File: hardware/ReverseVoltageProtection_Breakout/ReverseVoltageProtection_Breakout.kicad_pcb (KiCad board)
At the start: 2 copper layers, 33.5 x 17.8 mm, 5 parts, among them Q1 Q_PMOS_DGS

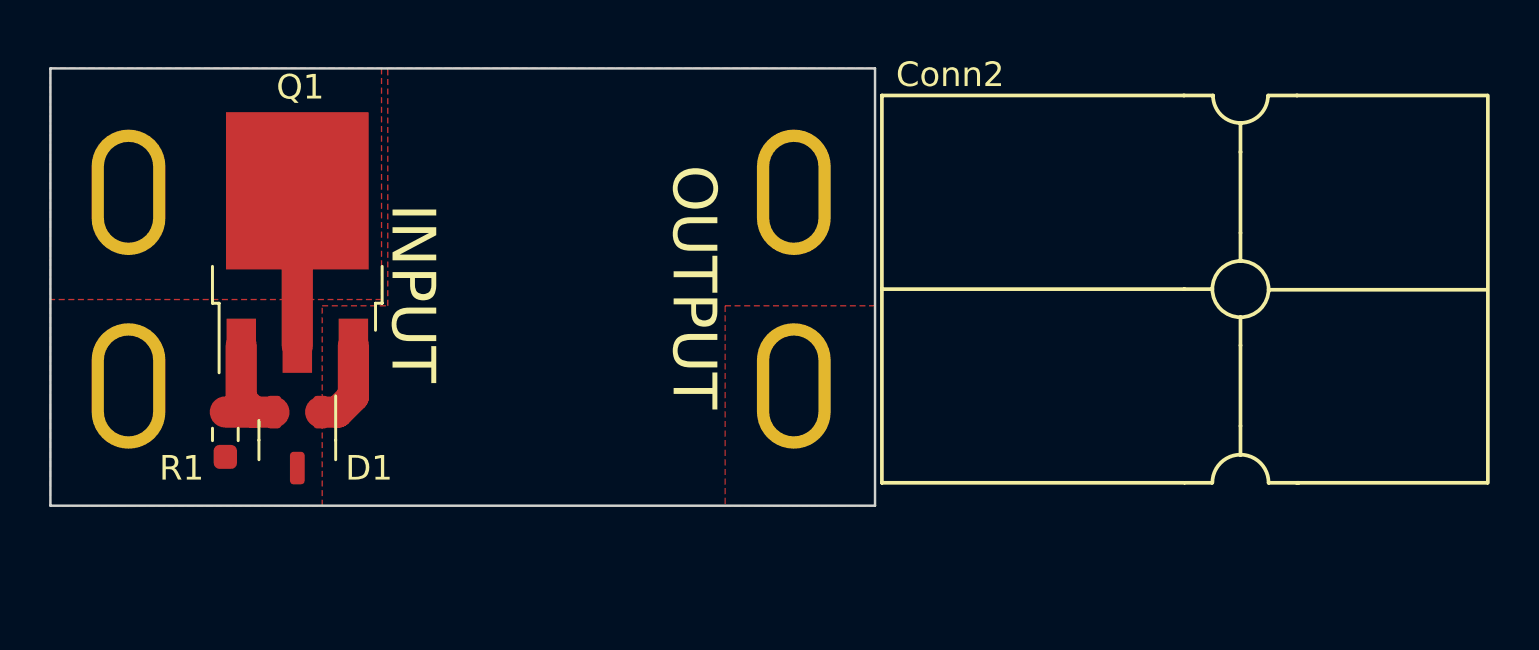
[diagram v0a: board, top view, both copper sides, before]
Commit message: made 12V version
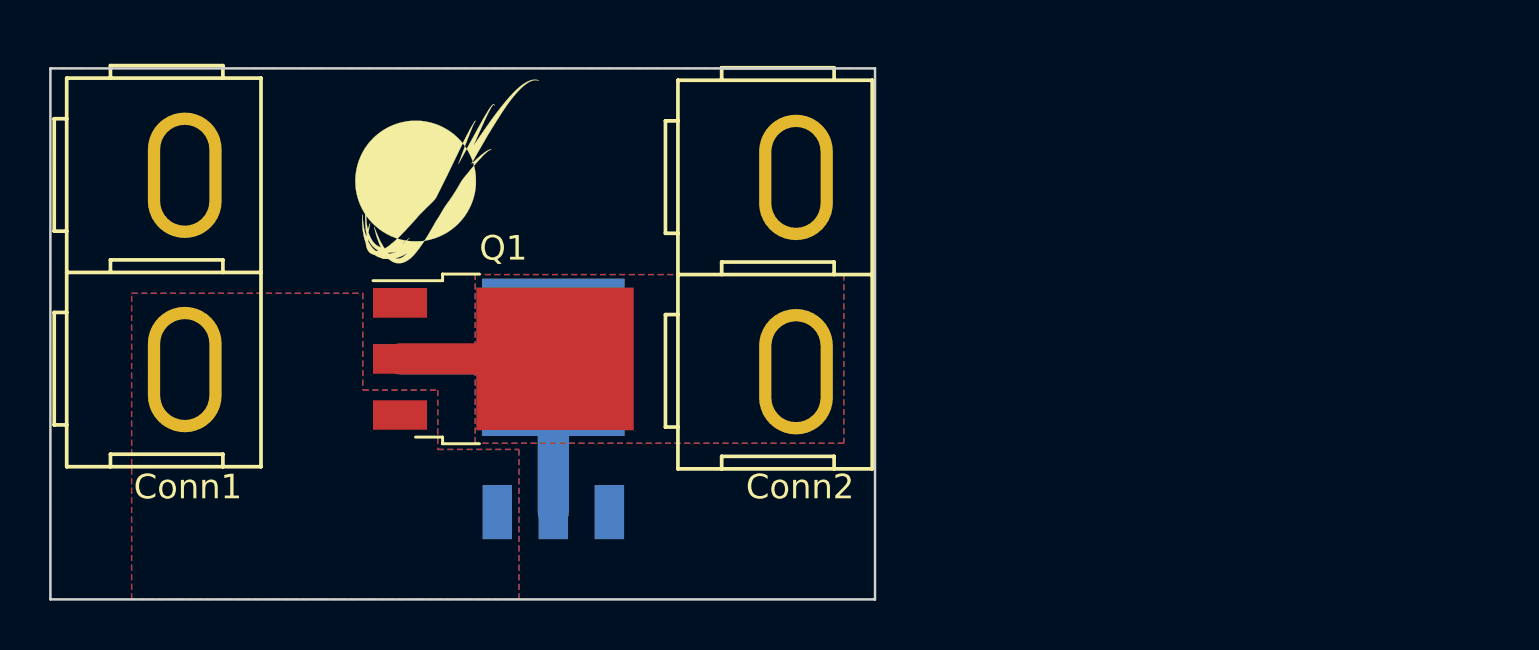
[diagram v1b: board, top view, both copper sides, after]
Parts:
- removed D1: D_Zener, Package_TO_SOT_SMD:SOT-23-3
- removed R1: 100k, Resistor_SMD:R_0603_1608Metric_Pad0.98x0.95mm_HandSolder
- added G***: LOGO, MRDT_Silkscreens:0_MRDT_Logo_7.5mm, F.Cu at (100.5, 108.8)
- added Q2: Q_PMOS_GDS, Package_TO_SOT_SMD:TO-252-3_TabPin2, B.Cu at (104.8, 118.5)
- Conn1: footprint MRDT_Connectors:Square_Anderson_2_H_Side_By_Side -> MRDT_Connectors:Square_Anderson_2_V_Side_By_Side; moved to F.Cu
- Conn2: footprint MRDT_Connectors:Square_Anderson_2_H_Side_By_Side -> MRDT_Connectors:Square_Anderson_2_V_Side_By_Side
- Q1: value Q_PMOS_DGS -> Q_PMOS_GDS
- moved Q1 9.62 mm to (102.7, 116.5), turned to 0 degrees
- moved Conn1 5.47 mm to (89.9, 113.0), turned to -90 degrees
- moved Conn2 5.03 mm to (114.8, 113.1), turned to -90 degrees
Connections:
- Conn1 pad 2: Net-(Conn1-Pad3) -> Net-(Conn1-Pad2)
- Conn2 pad 2: Net-(Conn2-Pad3) -> +12V
- Q1 pad 1: Net-(D1-Pad2) -> GND
- Q1 pad 2: Net-(Conn1-Pad3) -> +12V
- Q1 pad 3: Net-(Conn2-Pad3) -> Net-(Conn1-Pad2)
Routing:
- net +12V: track 0.00 -> 12.6 mm
- net Net-(Conn1-Pad3): track 6.30 -> 0.00 mm
- net Net-(D1-Pad2): track 4.88 -> 0.00 mm
- net Net-(Conn2-Pad3): track 3.65 -> 0.00 mm
- added copper zone on B.Cu, net +12V
- added copper zone on F.Cu, net +12V
- added copper zone on B.Cu, net Net-(Conn1-Pad2)
- added copper zone on F.Cu, net Net-(Conn1-Pad2)
- removed copper zone on F.Cu, net Net-(Conn1-Pad3)
- removed copper zone on F.Cu, net Net-(Conn2-Pad3)
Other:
- board size 33.5 x 17.8 mm -> 33.5 x 21.6 mm
- board text added: "12V RVP Board, Rev1 Mars Rover Design Team Missouri S&T 2023 Grant Brinker"
- board text added: "Board +"
- board text added: "Board -"
- board text added: "Wire +"
- board text added: "Wire -"
- board text removed: "INPUT"
- board text removed: "OUTPUT"
